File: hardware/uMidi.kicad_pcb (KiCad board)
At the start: 2 copper layers, 66 x 40.6 mm, 59 parts, among them CON1 USB-MINI-B, IC1 ATXMEGA128A4U-M, IC2 74LS14, IC3 LT1129CST-3.3, IC4 6N138, P1 MIDI In, P2 MIDI Thru, P3 MIDI T/O, P4 MIDI Out, P5 5..12 V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

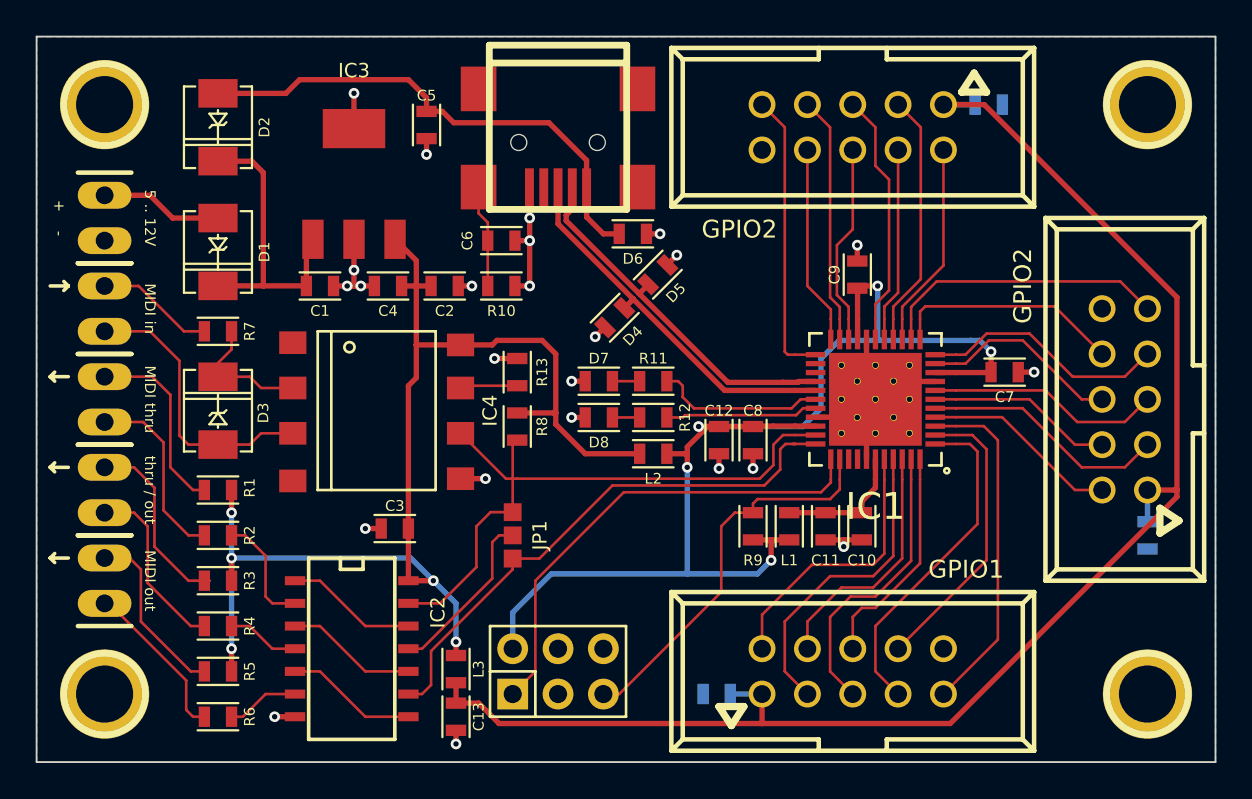
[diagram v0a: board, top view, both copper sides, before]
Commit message: Optimize cap placement around MCU
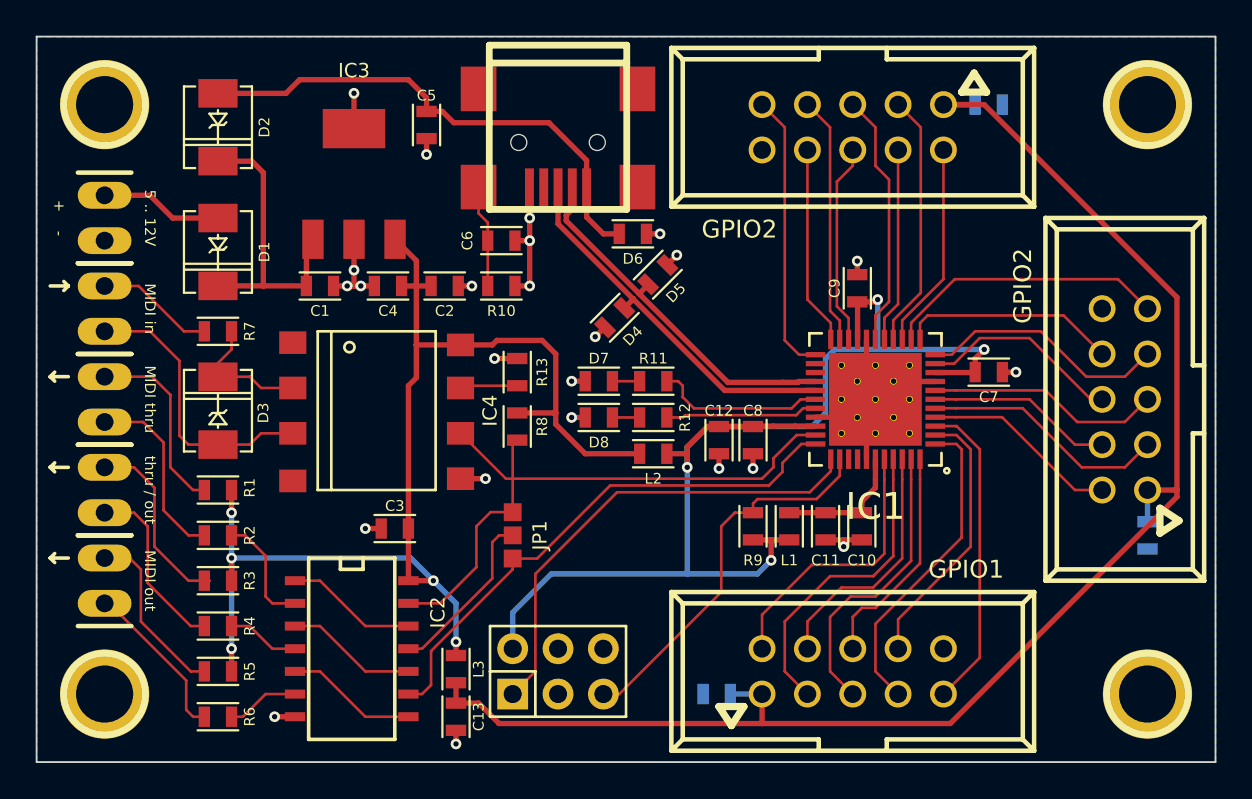
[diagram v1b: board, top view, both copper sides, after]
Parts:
- moved C7 0.89 mm to (120.7, 142.0)
- moved C9 0.76 mm to (113.3, 137.3)
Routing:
- net Net-(IC1-Pad3): track 19.3 -> 17.6 mm
- net Net-(C12-Pad1): track 70.8 -> 69.2 mm, vias 5 -> 4
- net Net-(IC1-Pad2): track 16.4 -> 15.2 mm
- net Net-(IC1-Pad1): track 19.0 -> 17.8 mm
- net Net-(IC1-Pad12): track 13.0 -> 12.2 mm
- net TXD: track 30.9 -> 30.4 mm

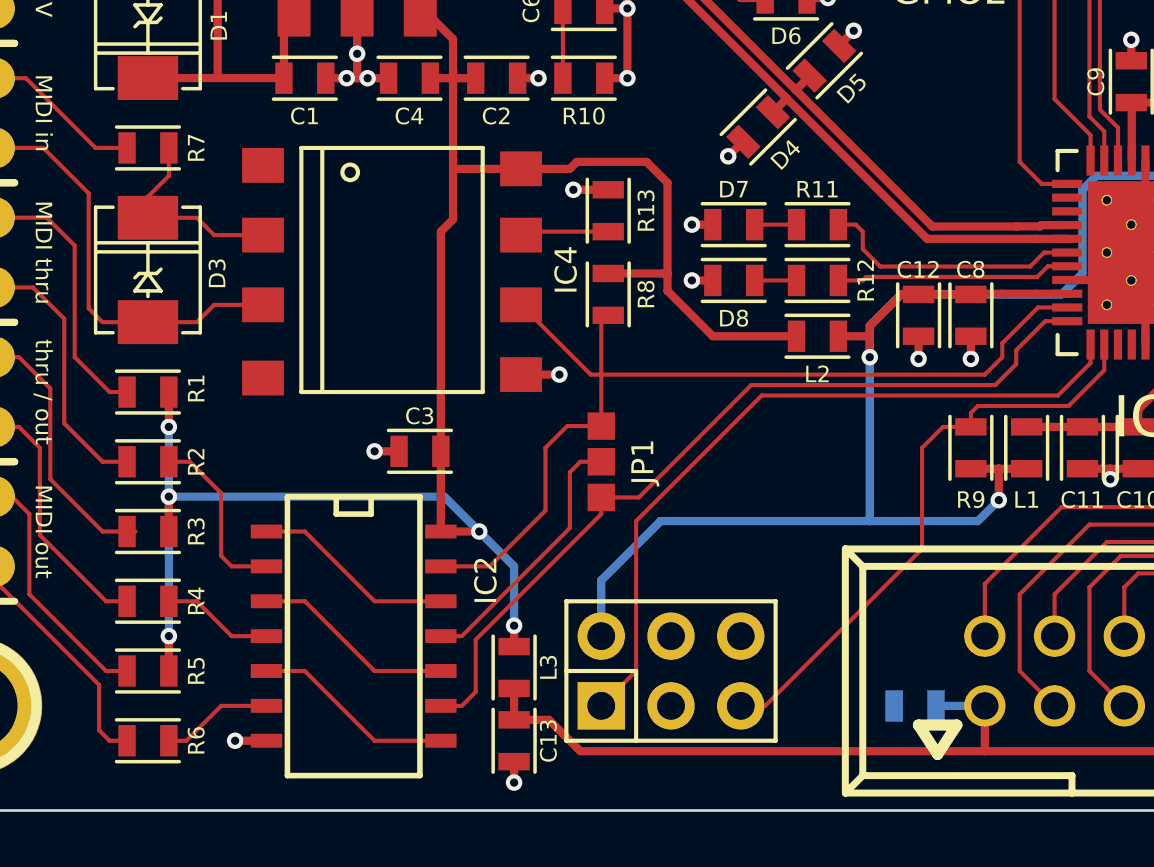
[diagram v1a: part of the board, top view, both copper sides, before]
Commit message: Integrate new SO14 footprint into PCB
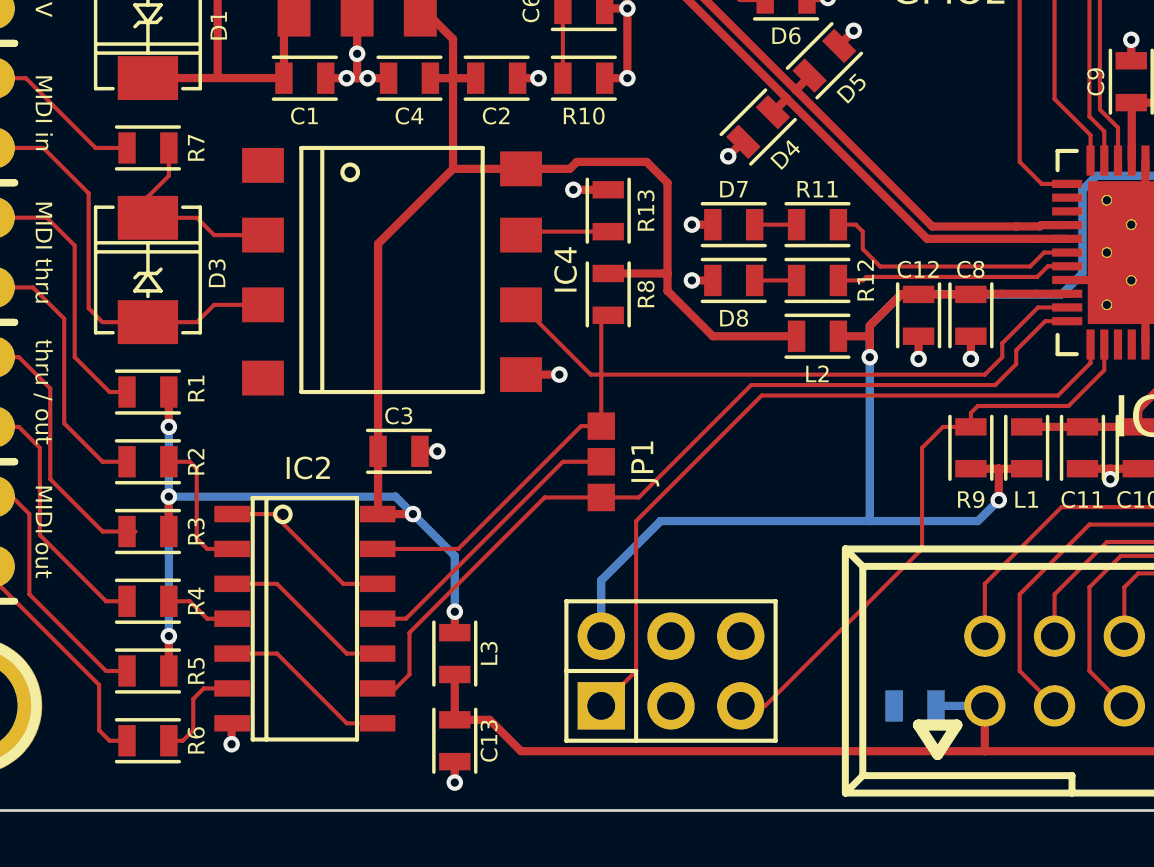
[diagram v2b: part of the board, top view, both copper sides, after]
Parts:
- IC2: footprint SMD_Packages:SOIC-14_N -> SMD:SOIC-14_N
- moved L3 2.22 mm to (88.6, 158.1)
- moved C13 2.16 mm to (88.6, 161.3)
- moved IC2 2.01 mm to (83.2, 156.8)
- moved C3 0.76 mm to (86.6, 150.7), turned to 0 degrees
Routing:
- net VGPIO: track 84.9 -> 87.5 mm
- net +3.3V: track 71.0 -> 68.8 mm
- net Net-(IC2-Pad4): track 4.08 -> 2.57 mm
- net TXD: track 30.4 -> 31.8 mm
- net Net-(IC2-Pad2): track 6.47 -> 5.11 mm
- net Net-(IC2-Pad1): track 7.40 -> 6.35 mm
- net Net-(IC2-Pad5): track 7.40 -> 6.35 mm
- net Net-(IC2-Pad10): track 7.40 -> 6.35 mm
- net Net-(IC2-Pad11): track 9.66 -> 10.5 mm
- net RXD: track 35.7 -> 36.4 mm
- net GND: track 45.2 -> 44.5 mm

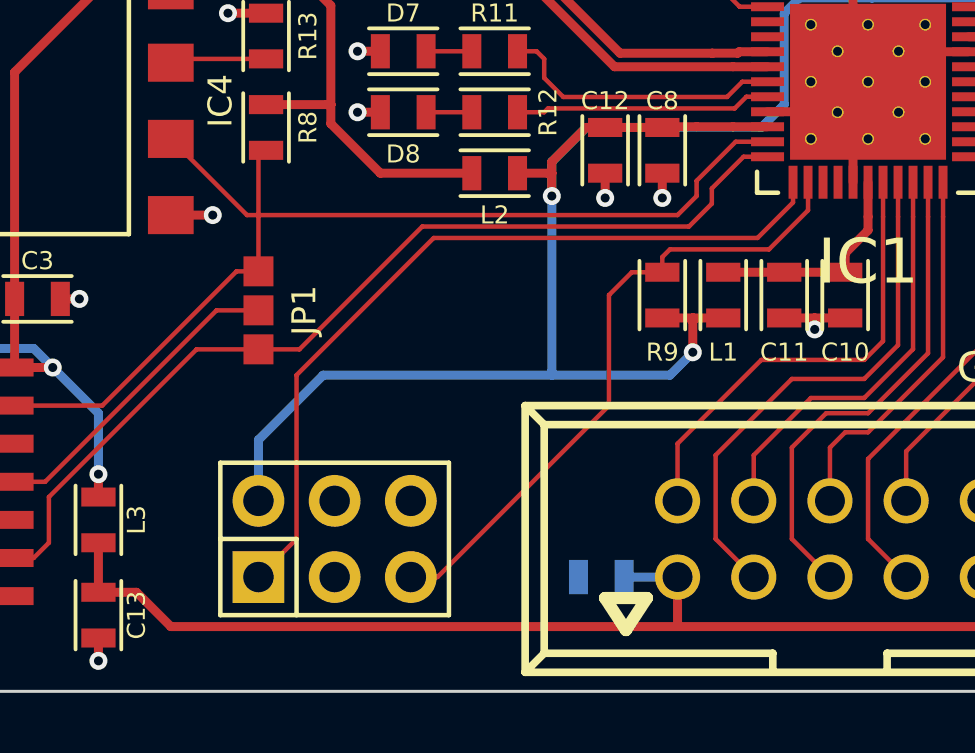
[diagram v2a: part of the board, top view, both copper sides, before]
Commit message: Increase spacing of PDI connector
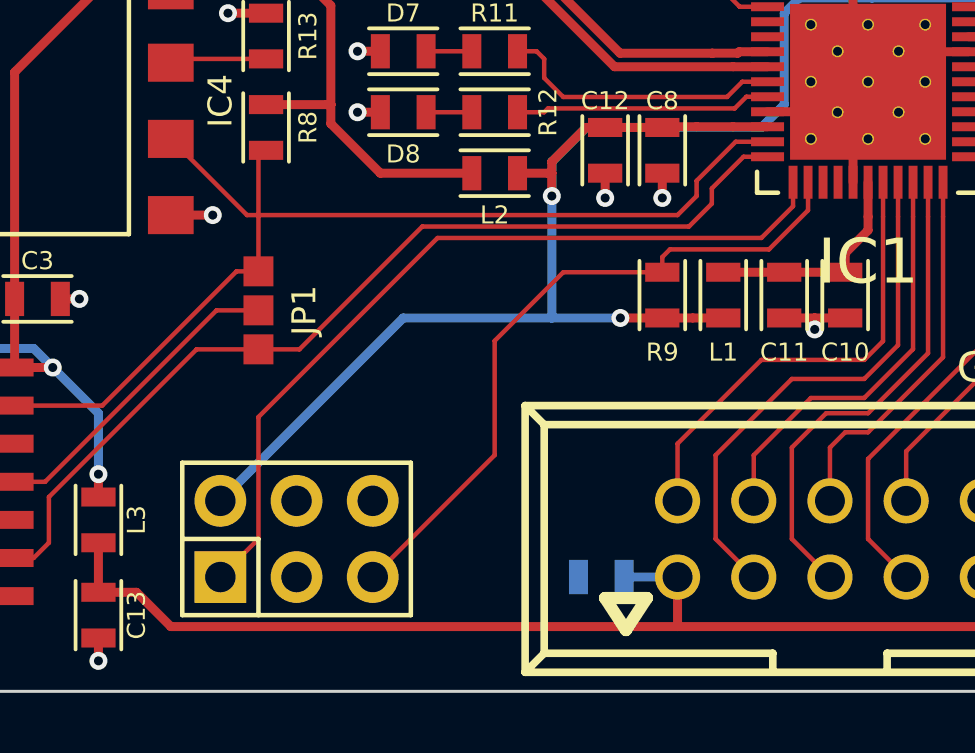
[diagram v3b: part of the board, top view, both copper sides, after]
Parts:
- moved P6 1.27 mm to (95.2, 158.8)
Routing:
- net Net-(C12-Pad1): track 69.2 -> 65.2 mm
- net Net-(IC1-Pad35): track 21.7 -> 23.0 mm
- net Net-(IC1-Pad34): track 26.9 -> 27.4 mm
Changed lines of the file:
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@@
     (thickness 1.6)
     (drawings 22)
-    (tracks 484)
+    (tracks 477)
     (zones 0)
     (modules 59)
@@
   )
   (module Pin_Headers:Pin_Header_Straight_2x03 placed (layer F.Cu)
-    (at 96.52 158.75)
+    (at 95.25 158.75)
     (descr "Through hole pin header")
     (tags "pin header")
@@
   (segment (start 82.41792 137.15492) (end 82.423 137.16) (width 0.3) (layer F.Cu) (net 1))
   (segment (start 82.588 134.747) (end 82.79 134.545) (width 0.3) (layer F.Cu) (net 1) (status 30))
-  (segment (start 88.646 162.052) (end 88.646 162.814) (width 0.3) (layer F.Cu) (net 2) (status 400000))
+  (segment (start 88.646 162.052) (end 88.646 162.814) (width 0.3) (layer F.Cu) (net 2))
   (via (at 88.646 162.814) (size 0.6) (layers F.Cu B.Cu) (net 2))
-  (segment (start 80.535 160.655) (end 80.518 160.672) (width 0.3) (layer F.Cu) (net 2) (status C00000))
-  (segment (start 80.518 160.672) (end 80.518 161.417) (width 0.3) (layer F.Cu) (net 2) (status 400000))
+  (segment (start 80.535 160.655) (end 80.518 160.672) (width 0.3) (layer F.Cu) (net 2))
+  (segment (start 80.518 160.672) (end 80.518 161.417) (width 0.3) (layer F.Cu) (net 2))
   (via (at 80.518 161.417) (size 0.6) (layers F.Cu B.Cu) (net 2))
   (segment (start 87.376 150.749) (end 88.011 150.749) (width 0.3) (layer F.Cu) (net 2))
@@
   (segment (start 114.3 148.01) (end 114.3 148.463) (width 0.3) (layer F.Cu) (net 4))
   (segment (start 114.3 148.463) (end 113.538 149.225) (width 0.3) (layer F.Cu) (net 4))
+  (segment (start 103.759 151.384) (end 98.806 151.384) (width 0.3) (layer B.Cu) (net 5))
+  (segment (start 98.806 151.384) (end 92.71 157.48) (width 0.3) (layer B.Cu) (net 5))
+  (segment (start 103.759 151.384) (end 103.759 147.32) (width 0.3) (layer B.Cu) (net 5))
+  (segment (start 106.045 151.384) (end 103.759 151.384) (width 0.3) (layer B.Cu) (net 5))
+  (via (at 106.045 151.384) (size 0.6) (layers F.Cu B.Cu) (net 5))
+  (segment (start 107.442 151.384) (end 106.045 151.384) (width 0.3) (layer F.Cu) (net 5))
   (segment (start 110.95 145.01) (end 109.8 145.01) (width 0.3) (layer F.Cu) (net 5))
   (segment (start 108.585 145.01) (end 107.466 145.01) (width 0.3) (layer F.Cu) (net 5))
   (segment (start 109.8 145.01) (end 108.585 145.01) (width 0.3) (layer F.Cu) (net 5))
-  (segment (start 103.759 147.32) (end 103.759 153.289) (width 0.3) (layer B.Cu) (net 5))
   (segment (start 103.759 146.558) (end 103.759 147.32) (width 0.3) (layer F.Cu) (net 5))
   (via (at 103.759 147.32) (size 0.6) (layers F.Cu B.Cu) (net 5))
-  (segment (start 103.759 153.289) (end 103.759 153.162) (width 0.3) (layer B.Cu) (net 5))
-  (segment (start 103.759 153.162) (end 103.759 153.289) (width 0.3) (layer B.Cu) (net 5))
-  (segment (start 93.98 157.48) (end 93.98 155.448) (width 0.3) (layer B.Cu) (net 5))
-  (segment (start 93.98 155.448) (end 96.139 153.289) (width 0.3) (layer B.Cu) (net 5))
-  (segment (start 96.139 153.289) (end 103.759 153.289) (width 0.3) (layer B.Cu) (net 5))
-  (segment (start 108.458 152.527) (end 108.458 151.384) (width 0.3) (layer F.Cu) (net 5))
-  (segment (start 103.759 153.289) (end 107.696 153.289) (width 0.3) (layer B.Cu) (net 5))
-  (segment (start 107.696 153.289) (end 108.458 152.527) (width 0.3) (layer B.Cu) (net 5))
-  (via (at 108.458 152.527) (size 0.6) (layers F.Cu B.Cu) (net 5))
-  (segment (start 108.458 151.384) (end 108.458 151.511) (width 0.3) (layer F.Cu) (net 5))
-  (segment (start 108.458 151.511) (end 108.458 151.384) (width 0.3) (layer F.Cu) (net 5))
   (segment (start 107.466 145.01) (end 107.442 145.034) (width 0.3) (layer F.Cu) (net 5))
   (segment (start 107.442 145.034) (end 105.537 145.034) (width 0.3) (layer F.Cu) (net 5))
@@
   (segment (start 113.284 138.049) (end 114.3 138.049) (width 0.3) (layer F.Cu) (net 5))
   (segment (start 103.759 146.177) (end 104.902 145.034) (width 0.3) (layer B.Cu) (net 5))
+  (segment (start 103.759 147.32) (end 103.759 146.177) (width 0.3) (layer B.Cu) (net 5))
+  (segment (start 112.014 140.716) (end 114.427 140.716) (width 0.3) (layer B.Cu) (net 5))
+  (segment (start 111.506 141.224) (end 112.014 140.716) (width 0.3) (layer B.Cu) (net 5))
+  (segment (start 111.506 144.272) (end 111.506 141.224) (width 0.3) (layer B.Cu) (net 5))
+  (segment (start 110.744 145.034) (end 111.506 144.272) (width 0.3) (layer B.Cu) (net 5))
   (segment (start 104.902 145.034) (end 110.744 145.034) (width 0.3) (layer B.Cu) (net 5))
-  (segment (start 110.744 145.034) (end 111.506 144.272) (width 0.3) (layer B.Cu) (net 5))
-  (segment (start 111.506 144.272) (end 111.506 141.224) (width 0.3) (layer B.Cu) (net 5))
-  (segment (start 111.506 141.224) (end 112.014 140.716) (width 0.3) (layer B.Cu) (net 5))
-  (segment (start 112.014 140.716) (end 114.427 140.716) (width 0.3) (layer B.Cu) (net 5))
-  (segment (start 103.759 147.32) (end 103.759 146.177) (width 0.3) (layer B.Cu) (net 5))
   (segment (start 109.1057 142.5575) (end 109.9566 142.5575) (width 0.3) (layer F.Cu) (net 6))
   (segment (start 110.0041 142.51) (end 110.95 142.51) (width 0.3) (layer F.Cu) (net 6))
@@
   (segment (start 95.347 152.43) (end 93.98 152.43) (width 0.15) (layer F.Cu) (net 37))
   (segment (start 110.95 146.01) (end 110.149 146.01) (width 0.15) (layer F.Cu) (net 37))
-  (segment (start 111.8 147.534) (end 110.617 148.717) (width 0.15) (layer F.Cu) (net 38))
-  (segment (start 110.617 148.717) (end 99.822 148.717) (width 0.15) (layer F.Cu) (net 38))
-  (segment (start 99.822 148.717) (end 95.25 153.289) (width 0.15) (layer F.Cu) (net 38))
-  (segment (start 95.25 153.289) (end 95.25 158.75) (width 0.15) (layer F.Cu) (net 38))
-  (segment (start 95.25 158.75) (end 93.98 160.02) (width 0.15) (layer F.Cu) (net 38))
-  (segment (start 111.8 146.86) (end 111.8 147.534) (width 0.15) (layer F.Cu) (net 38))
-  (segment (start 99.06 160.02) (end 99.949 160.02) (width 0.15) (layer F.Cu) (net 39))
-  (segment (start 106.426 149.86) (end 107.442 149.86) (width 0.15) (layer F.Cu) (net 39))
-  (segment (start 105.664 150.622) (end 106.426 149.86) (width 0.15) (layer F.Cu) (net 39))
-  (segment (start 105.664 154.305) (end 105.664 150.622) (width 0.15) (layer F.Cu) (net 39))
-  (segment (start 99.949 160.02) (end 105.664 154.305) (width 0.15) (layer F.Cu) (net 39))
+  (segment (start 92.71 160.02) (end 93.98 158.75) (width 0.15) (layer F.Cu) (net 38))
+  (segment (start 111.8 147.661) (end 111.8 146.86) (width 0.15) (layer F.Cu) (net 38))
+  (segment (start 110.744 148.717) (end 111.8 147.661) (width 0.15) (layer F.Cu) (net 38))
+  (segment (start 99.949 148.717) (end 110.744 148.717) (width 0.15) (layer F.Cu) (net 38))
+  (segment (start 93.98 154.686) (end 99.949 148.717) (width 0.15) (layer F.Cu) (net 38))
+  (segment (start 93.98 158.75) (end 93.98 154.686) (width 0.15) (layer F.Cu) (net 38))
+  (segment (start 97.79 160.02) (end 101.854 155.956) (width 0.15) (layer F.Cu) (net 39))
+  (segment (start 104.14 149.86) (end 107.442 149.86) (width 0.15) (layer F.Cu) (net 39))
+  (segment (start 101.854 152.146) (end 104.14 149.86) (width 0.15) (layer F.Cu) (net 39))
+  (segment (start 101.854 155.956) (end 101.854 152.146) (width 0.15) (layer F.Cu) (net 39))
   (segment (start 112.3 147.796) (end 110.998 149.098) (width 0.15) (layer F.Cu) (net 39))
   (segment (start 110.998 149.098) (end 107.696 149.098) (width 0.15) (layer F.Cu) (net 39))
@@
   (segment (start 92.06992 133.09092) (end 92.583 133.604) (width 0.15) (layer F.Cu) (net 60))
   (segment (start 107.95 161.671) (end 91.059 161.671) (width 0.3) (layer F.Cu) (net 63))
-  (segment (start 89.916 160.528) (end 88.646 160.528) (width 0.3) (layer F.Cu) (net 63) (status 800000))
+  (segment (start 89.916 160.528) (end 88.646 160.528) (width 0.3) (layer F.Cu) (net 63))
   (segment (start 91.059 161.671) (end 89.916 160.528) (width 0.3) (layer F.Cu) (net 63))
   (segment (start 88.646 158.877) (end 88.646 160.528) (width 0.3) (layer F.Cu) (net 63))
